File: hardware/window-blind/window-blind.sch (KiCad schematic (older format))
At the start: 31 parts, among them IC1 ATMEGA48PA-A, P1 CONN_02X03, SW1 UP, SW2 DN, SW3 END1, SW4 END2, U1 SP3485CN, U2 L298N, U3 LM78L05ACZ, Y1 16M

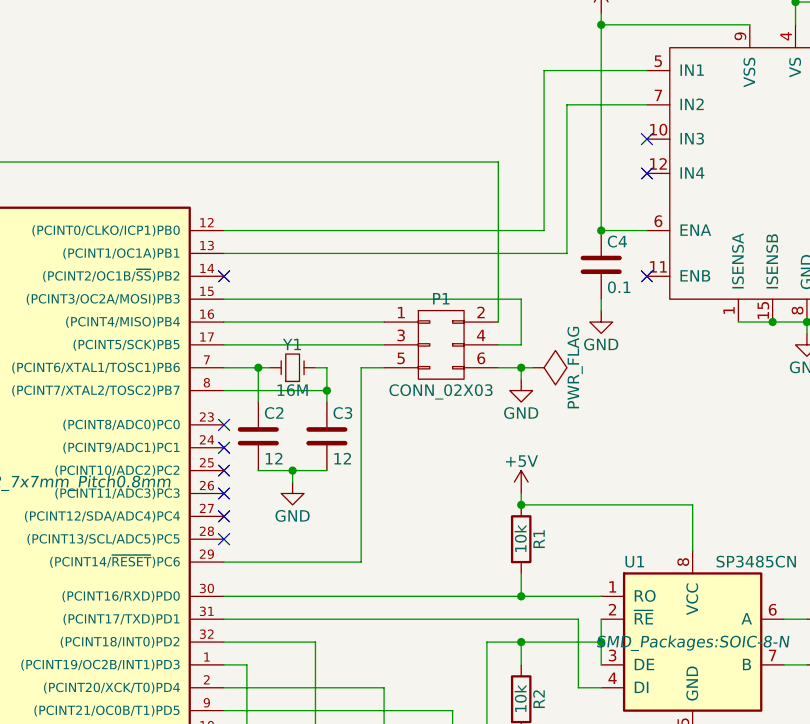
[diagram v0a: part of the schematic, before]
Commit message: Built sunblind PCB layout
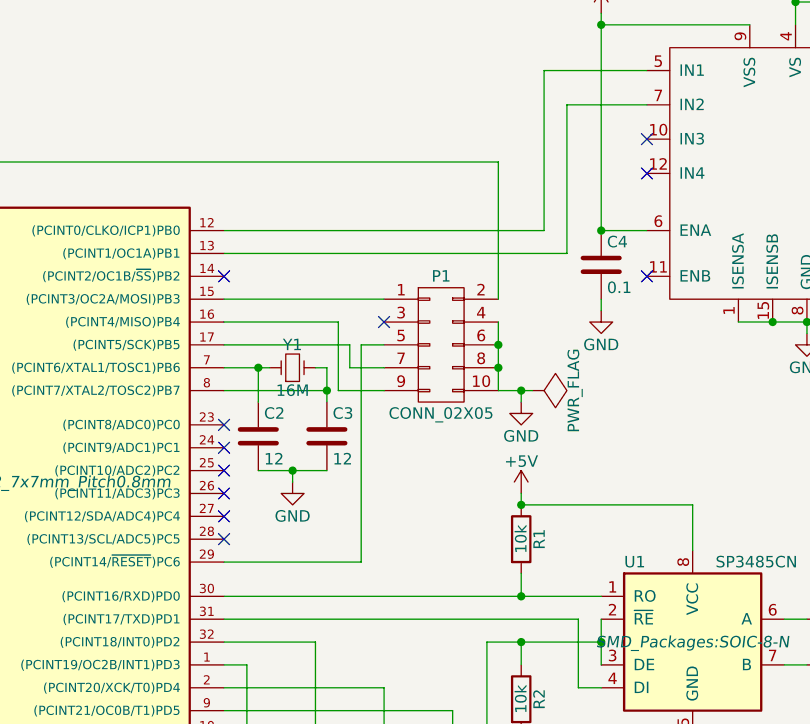
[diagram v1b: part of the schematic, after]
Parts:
- removed P1: CONN_02X03, Pin_Headers:Pin_Header_Straight_2x03, symbol CONN_02X03
- added P1: CONN_02X05, Pin_Headers:Pin_Header_Straight_2x05, symbol CONN_02X05
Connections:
- net +5V: now also P1.2 (P2)
- net GND: now also P1.10 (P10), P1.4 (P4), P1.6 (P6), P1.8 (P8)
- net at IC1.15 ((PCINT3/OC2A/MOSI)PB3): now also P1.1 (P1)
- net at IC1.16 ((PCINT4/MISO)PB4): now also P1.9 (P9)
- net at IC1.17 ((PCINT5/SCK)PB5): now also P1.7 (P7)
- net at IC1.29 ((PCINT14/~RESET~)PC6): now also P1.5 (P5)
- no-connect marks 17 -> 18
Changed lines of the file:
@@
-$EndComp
-$Comp
-L CONN_02X03 P1
-U 1 1 571BEC1C
-P 4650 3650
-F 0 "P1" H 4650 3850 50  0000 C CNN
-F 1 "CONN_02X03" H 4650 3450 50  0000 C CNN
-F 2 "Pin_Headers:Pin_Header_Straight_2x03" H 4650 2450 50  0001 C CNN
-F 3 "" H 4650 2450 50  0000 C CNN
-	1    4650 3650
-	1    0    0    -1
 $EndComp
 $Comp
 L GND #PWR01
 U 1 1 571BEDC7
-P 5000 3800
-F 0 "#PWR01" H 5000 3550 50  0001 C CNN
-F 1 "GND" H 5000 3650 50  0000 C CNN
-F 2 "" H 5000 3800 50  0000 C CNN
-F 3 "" H 5000 3800 50  0000 C CNN
-	1    5000 3800
+P 5000 3900
+F 0 "#PWR01" H 5000 3650 50  0001 C CNN
+F 1 "GND" H 5000 3750 50  0000 C CNN
+F 2 "" H 5000 3900 50  0000 C CNN
+F 3 "" H 5000 3900 50  0000 C CNN
+	1    5000 3900
 	1    0    0    -1
 $EndComp
@@
 L PWR_FLAG #FLG02
 U 1 1 571BEDDF
-P 5050 3750
-F 0 "#FLG02" H 5050 3845 50  0001 C CNN
-F 1 "PWR_FLAG" H 5050 3930 50  0000 C CNN
-F 2 "" H 5050 3750 50  0000 C CNN
-F 3 "" H 5050 3750 50  0000 C CNN
-	1    5050 3750
+P 5050 3850
+F 0 "#FLG02" H 5050 3945 50  0001 C CNN
+F 1 "PWR_FLAG" H 5050 4030 50  0000 C CNN
+F 2 "" H 5050 3850 50  0000 C CNN
+F 3 "" H 5050 3850 50  0000 C CNN
+	1    5050 3850
 	0    1    1    0
 $EndComp
@@
 $EndComp
 Wire Wire Line
-	3700 3550 4400 3550
-Wire Wire Line
-	3700 3650 4400 3650
-Wire Wire Line
-	3700 4600 4300 4600
-Wire Wire Line
-	4300 4600 4300 3750
-Wire Wire Line
-	4300 3750 4400 3750
-Wire Wire Line
-	3700 3450 5000 3450
-Wire Wire Line
-	5000 3450 5000 3650
-Wire Wire Line
-	5000 3650 4900 3650
-Wire Wire Line
-	4900 3750 5050 3750
-Wire Wire Line
-	5000 3800 5000 3750
-Connection ~ 5000 3750
+	4300 4600 3700 4600
+Wire Wire Line
+	4300 3650 4300 4600
 Wire Wire Line
 	1500 3550 1500 3650
@@
 Wire Wire Line
 	1500 2850 4900 2850
-Wire Wire Line
-	4900 2850 4900 3550
 Connection ~ 1500 3250
 Wire Wire Line
@@
 	4000 4250 4000 4200
 Connection ~ 4000 4200
+$Comp
+L CONN_02X05 P1
+U 1 1 571D79C9
+P 4650 3650
+F 0 "P1" H 4650 3950 50  0000 C CNN
+F 1 "CONN_02X05" H 4650 3350 50  0000 C CNN
+F 2 "Pin_Headers:Pin_Header_Straight_2x05" H 4650 2450 50  0001 C CNN
+F 3 "" H 4650 2450 50  0000 C CNN
+	1    4650 3650
+	1    0    0    -1
+$EndComp
+Wire Wire Line
+	3700 3450 4400 3450
+NoConn ~ 4400 3550
+Wire Wire Line
+	4400 3650 4300 3650
+Wire Wire Line
+	3700 3650 4250 3650
+Wire Wire Line
+	4250 3650 4250 3750
+Wire Wire Line
+	4250 3750 4400 3750
+Wire Wire Line
+	4400 3850 4200 3850
+Wire Wire Line
+	4200 3850 4200 3550
+Wire Wire Line
+	4200 3550 3700 3550
+Wire Wire Line
+	4900 3550 4900 3850
+Wire Wire Line
+	4900 3850 5050 3850
+Wire Wire Line
+	5000 3900 5000 3850
+Connection ~ 5000 3850
+Connection ~ 4900 3650
+Connection ~ 4900 3750
+Wire Wire Line
+	4900 2850 4900 3450
 $EndSCHEMATC
